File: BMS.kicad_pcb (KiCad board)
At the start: 2 copper layers, 78 parts, among them J1 Screw_Terminal_01x02, J5 BATT_PACK -, J6 PACK _PACK -, Q22 CSD19531Q5A, Q23 CSD19531Q5A, Q24 CSD19531Q5A, T3 EE20_10_6_750811647, U1 TL431DBZ, U18 VIPer26LD, U2 PC817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

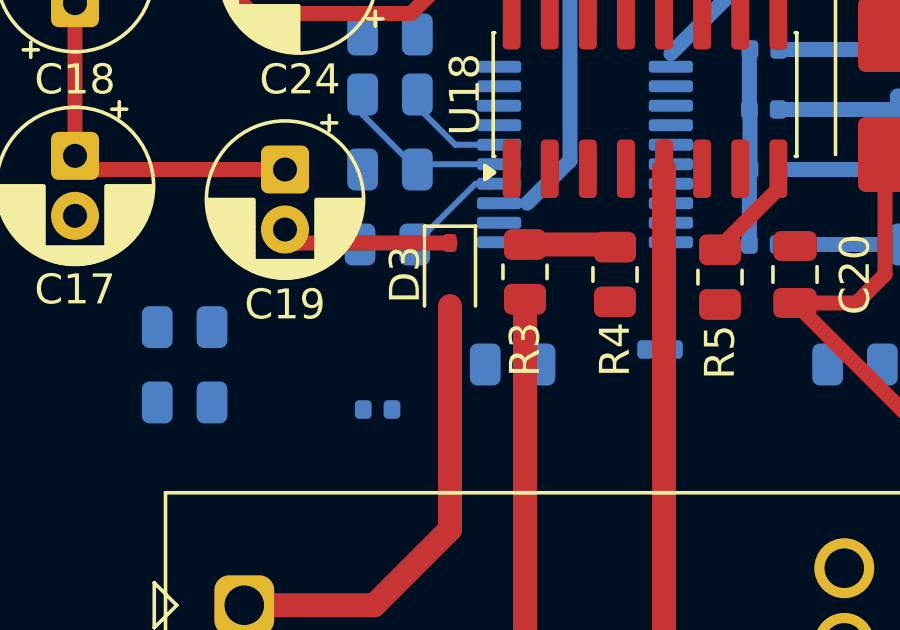
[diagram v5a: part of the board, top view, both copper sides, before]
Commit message: front layer route
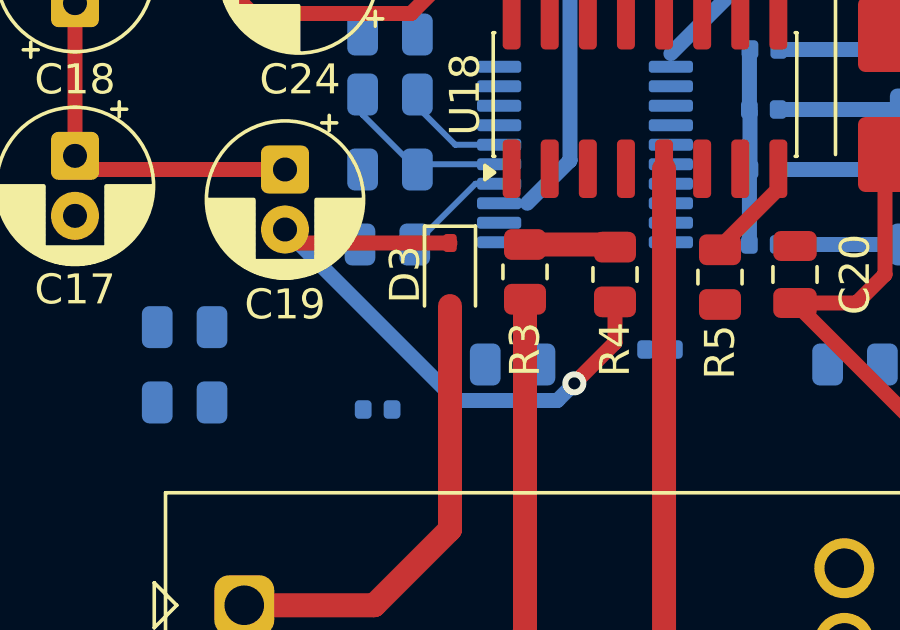
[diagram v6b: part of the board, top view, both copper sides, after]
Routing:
- net Net-(D3-K): track 5.69 -> 21.2 mm, vias 0 -> 1
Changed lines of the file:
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@@
+	)
+	(segment
+		(start 147.5 90.772915)
+		(end 146.14468 92.128235)
+		(width 0.5)
+		(layer "F.Cu")
+		(net "Net-(D3-K)")
 	)
 	(segment
@@
 		(net "Net-(D3-K)")
 	)
+	(segment
+		(start 147.5 89.4125)
+		(end 147.5 90.772915)
+		(width 0.5)
+		(layer "F.Cu")
+		(net "Net-(D3-K)")
+	)
+	(via
+		(at 146.14468 92.128235)
+		(size 0.8)
+		(drill 0.4)
+		(layers "F.Cu" "B.Cu")
+		(net "Net-(D3-K)")
+	)
+	(segment
+		(start 145.580088 92.7)
+		(end 142.2 92.7)
+		(width 0.5)
+		(layer "B.Cu")
+		(net "Net-(D3-K)")
+	)
+	(segment
+		(start 146.14468 92.135408)
+		(end 145.580088 92.7)
+		(width 0.5)
+		(layer "B.Cu")
+		(net "Net-(D3-K)")
+	)
+	(segment
+		(start 142.2 92.7)
+		(end 136.5 87)
+		(width 0.5)
+		(layer "B.Cu")
+		(net "Net-(D3-K)")
+	)
+	(segment
+		(start 146.14468 92.128235)
+		(end 146.14468 92.135408)
+		(width 0.5)
+		(layer "B.Cu")
+		(net "Net-(D3-K)")
+	)

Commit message: Routing update
 19 errors to go
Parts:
- removed J6: PACK _PACK -, TerminalBlock_MetzConnect:TerminalBlock_MetzConnect_360271_1x01_Horizontal_ScrewM3.0_Boxed
- added RV1: R_Pot_Trim, Resistor_SMD:R_0805_2012Metric, B.Cu at (134.0, 51.0)
- added RV2: R_Pot_Trim, Potentiometer_SMD:Potentiometer_ACP_CA6-VSMD_Vertical, B.Cu at (153.0, 57.0)
- added RV3: R_Pot_Trim, Potentiometer_SMD:Potentiometer_ACP_CA6-VSMD_Vertical, B.Cu at (130.0, 45.0)
- 10k2: moved to F.Cu
- moved J5 79.3 mm to (181.0, 121.0)
- moved Q22 47.9 mm to (105.8, 61.9), turned to 180 degrees
- moved 10k2 46.1 mm to (142.0, 45.0), turned to 0 degrees
- moved 10k3 44.4 mm to (162.0, 59.0)
- moved R1 42.9 mm to (113.0, 63.0), turned to 180 degrees
- moved C3 37.8 mm to (168.0, 42.0)
- moved R6 28.8 mm to (128.0, 83.0)
- moved Q23 28.2 mm to (132.9, 83.6)
- moved Rsrp1 23.1 mm to (160.0, 92.1), turned to -90 degrees
- moved C37 12.9 mm to (152.5, 93.0)
- moved RVO1 11.9 mm to (158.0, 79.0)
- moved C30 6.13 mm to (158.0, 76.0), turned to 0 degrees
- moved C17 5.46 mm to (129.5, 90.0)
- moved C19 5.46 mm to (136.5, 90.5)
- moved U3 4.21 mm to (138.8, 42.2)
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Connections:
- U2 pad 1: VDD_U18 -> Net-(R12-Pad2)
- U2 pad 2: FB -> Net-(U1-K)
- U2 pad 3: Net-(U1-K) -> FB
- U2 pad 4: Net-(R12-Pad2) -> VDD_U18
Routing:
- net Net-(D11-K): track 0.00 -> 115.7 mm, vias 0 -> 4
- net Net-(D6-K): track 0.00 -> 99.3 mm, vias 0 -> 3
- net Net-(D8-K): track 0.00 -> 97.0 mm, vias 0 -> 2
- net Net-(D9-K): track 0.00 -> 95.5 mm, vias 0 -> 3
- net Net-(D10-A): track 0.38 -> 95.6 mm, vias 0 -> 1
- net Net-(D12-K): track 0.00 -> 92.8 mm, vias 0 -> 1
- net Net-(D13-K): track 0.00 -> 90.9 mm, vias 0 -> 1
- net Net-(D14-K): track 0.00 -> 90.5 mm, vias 0 -> 1
- net Net-(D10-K): track 0.00 -> 88.8 mm, vias 0 -> 1
- net Net-(D16-K): track 0.00 -> 87.2 mm, vias 0 -> 1
- net Net-(D15-K): track 0.00 -> 86.1 mm, vias 0 -> 1
- net V+: track 0.00 -> 78.3 mm, vias 0 -> 3
- net PACK-: track 0.00 -> 72.6 mm
- net Net-(BT16--): track 0.00 -> 69.8 mm
- net Net-(BT15-+): track 0.00 -> 67.9 mm
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- added copper zone on B.Cu, net GND
- added copper zone on F.Cu, net GND
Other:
- board outline added: 136.4 x 85.6 mm
